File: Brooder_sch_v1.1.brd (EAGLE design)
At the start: 90 x 75 mm, 31 parts, among them J1 DCJ0202, J2 1X2-3.5MM, J3 DCJ0202, J4 1X2-3.5MM, U1 328P

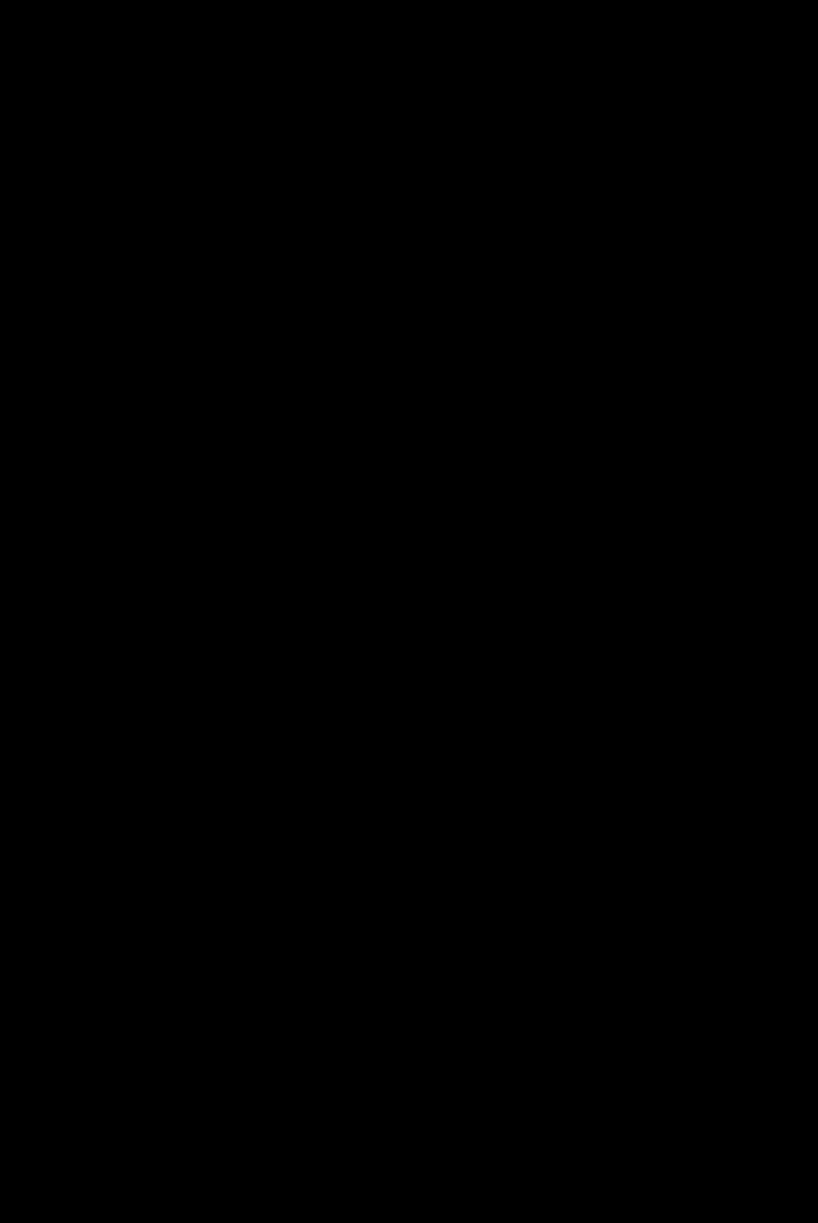
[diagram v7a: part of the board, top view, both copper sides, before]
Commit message: Adds extractor fan relay to schematic
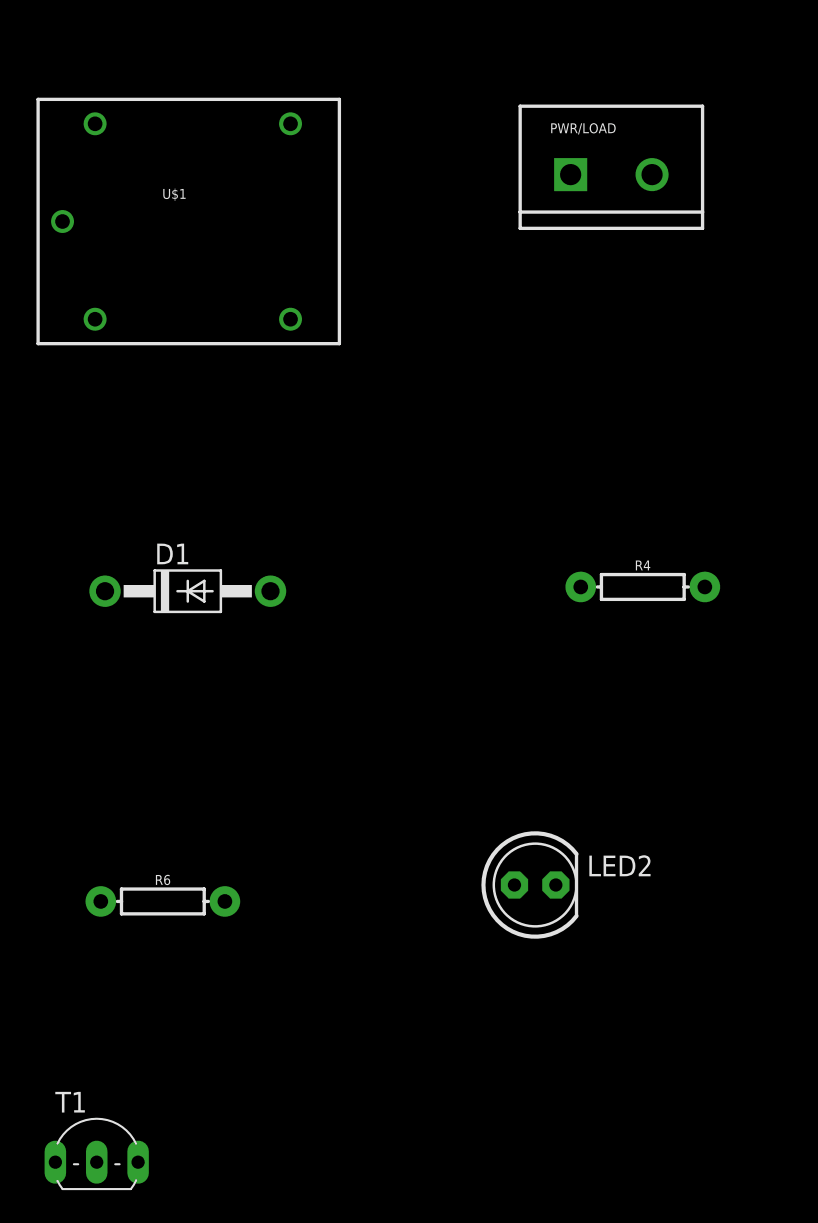
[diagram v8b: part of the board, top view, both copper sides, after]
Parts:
- added D1: 1N4007, adafruit:DO41-10
- added LED2: (no value), adafruit:LED5MM
- added PWR/LOAD: (no value), SparkFun-Connectors:SCREWTERMINAL-5MM-2
- added R4: 220, SparkFun-Resistors:AXIAL-0.3
- added R6: 1k, SparkFun-Resistors:AXIAL-0.3
- added T1: 2N2222, adafruit:TO92-EBC-OVAL
- added U$1: RELAYPTH, SRD-05VDC-SL-C:SRD-05VDC-SL-C
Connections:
- new net N$10: R6.P$1, T1.B
- new net N$13: PWR/LOAD.1, U$1.SWCLOSED
- new net N$14: PWR/LOAD.2, U$1.SWCOMMON
- new net N$6: D1.A, LED2.K, T1.C, U$1.COIL0
- new net N$7: LED2.A, R4.P$1
- net 5V: now also D1.C, R4.P$2, U$1.COIL1
- net GND: now also T1.E
- net PC1: now also R6.P$2
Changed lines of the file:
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@@
 <element name="R1" library="pot" library_urn="urn:adsk.eagle:library:331" package="CT6" package3d_urn="urn:adsk.eagle:package:22692/1" value="" x="14.57" y="58.36" rot="R270"/>
 <element name="JP1" library="pinhead" library_urn="urn:adsk.eagle:library:325" package="2X03" package3d_urn="urn:adsk.eagle:package:22462/2" value="" x="62.7" y="25.49" rot="R270"/>
+<element name="U$1" library="SRD-05VDC-SL-C" package="SRD-05VDC-SL-C" value="RELAYPTH" x="9.23" y="-24.48"/>
+<element name="D1" library="adafruit" package="DO41-10" value="1N4007" x="9.53" y="-47.3"/>
+<element name="T1" library="adafruit" package="TO92-EBC-OVAL" value="2N2222" x="3.94" y="-81.09"/>
+<element name="PWR/LOAD" library="SparkFun-Connectors" package="SCREWTERMINAL-5MM-2" value="" x="33.04" y="-21.72">
+<attribute name="SF_SKU" value="PRT-08432" x="4.96" y="-80.33" size="1.778" layer="27" display="off"/>
+</element>
+<element name="R4" library="SparkFun-Resistors" package="AXIAL-0.3" value="220" x="37.47" y="-47.04">
+<attribute name="PROD_ID" value="RES-09327" x="8" y="-99.89" size="1.778" layer="27" display="off"/>
+</element>
+<element name="R6" library="SparkFun-Resistors" package="AXIAL-0.3" value="1k" x="8" y="-66.35">
+<attribute name="PROD_ID" value="RES-09327" x="8" y="-118.69" size="1.778" layer="27" display="off"/>
+</element>
+<element name="LED2" library="adafruit" package="LED5MM" value="" x="30.86" y="-65.34"/>
 </elements>
 <signals>
@@
 <wire x1="72.1" y1="12.57" x2="70.81" y2="13.86" width="1.27" layer="16"/>
 <wire x1="70.81" y1="13.86" x2="67.58068125" y2="13.86" width="1.27" layer="16"/>
+<contactref element="T1" pad="E"/>
 <wire x1="15.02" y1="66.32" x2="34.4888" y2="66.7906" width="0" layer="19" extent="1-1"/>
 <wire x1="5" y1="7" x2="4.19" y2="14.85" width="0" layer="19" extent="16-16"/>
 <wire x1="20.24" y1="41.49" x2="13.87" y2="52.87" width="0" layer="19" extent="1-16"/>
 <wire x1="19.71" y1="34.8" x2="19.72" y2="39.62" width="0" layer="19" extent="1-1"/>
+<wire x1="1.4" y1="-82.36" x2="13" y2="2" width="0" layer="19" extent="16-16"/>
 </signal>
 <signal name="12V">
@@
 <wire x1="67.35" y1="62.01" x2="78.99" y2="62.01" width="1.27" layer="1"/>
 <wire x1="78.99" y1="62.01" x2="82.46" y2="58.54" width="1.27" layer="1"/>
+<contactref element="U$1" pad="COIL1"/>
+<contactref element="D1" pad="C"/>
+<contactref element="R4" pad="P$2"/>
+<wire x1="3.84" y1="-18.6" x2="4.45" y2="-47.3" width="0" layer="19" extent="1-1"/>
+<wire x1="41.28" y1="-47.04" x2="4.45" y2="-47.3" width="0" layer="19" extent="1-1"/>
+<wire x1="4.19" y1="19.93" x2="3.84" y2="-18.6" width="0" layer="19" extent="1-1"/>
 </signal>
 <signal name="N$5">
@@
 <wire x1="41.94" y1="46.37" x2="42.38" y2="46.81" width="1.27" layer="16"/>
 <wire x1="42.38" y1="46.81" x2="45" y2="46.81" width="1.27" layer="16"/>
+<contactref element="R6" pad="P$2"/>
+<wire x1="11.81" y1="-66.35" x2="41.94" y2="46.37" width="0" layer="19" extent="1-1"/>
 </signal>
 <signal name="PC4">
@@
 <wire x1="48.05" y1="26.05" x2="50.06" y2="24.04" width="1.27" layer="16"/>
 </signal>
+<signal name="N$6">
+<contactref element="D1" pad="A"/>
+<contactref element="U$1" pad="COIL0"/>
+<contactref element="LED2" pad="K"/>
+<contactref element="T1" pad="C"/>
+<wire x1="32.13" y1="-65.34" x2="6.48" y2="-82.36" width="0" layer="19" extent="1-1"/>
+<wire x1="14.61" y1="-47.3" x2="32.13" y2="-65.34" width="0" layer="19" extent="1-1"/>
+<wire x1="3.84" y1="-30.6" x2="14.61" y2="-47.3" width="0" layer="19" extent="1-1"/>
+</signal>
+<signal name="N$7">
+<contactref element="R4" pad="P$1"/>
+<contactref element="LED2" pad="A"/>
+<wire x1="33.66" y1="-47.04" x2="29.59" y2="-65.34" width="0" layer="19" extent="1-1"/>
+</signal>
+<signal name="N$10">
+<contactref element="R6" pad="P$1"/>
+<contactref element="T1" pad="B"/>
+<wire x1="4.19" y1="-66.35" x2="3.94" y2="-82.36" width="0" layer="19" extent="1-1"/>
+</signal>
+<signal name="N$13">
+<contactref element="PWR/LOAD" pad="1"/>
+<contactref element="U$1" pad="SWCLOSED"/>
+<wire x1="33.04" y1="-21.72" x2="15.84" y2="-30.6" width="0" layer="19" extent="1-1"/>
+</signal>
+<signal name="N$14">
+<contactref element="U$1" pad="SWCOMMON"/>
+<contactref element="PWR/LOAD" pad="2"/>
+<wire x1="38.04" y1="-21.72" x2="1.84" y2="-24.6" width="0" layer="19" extent="1-1"/>
+</signal>
 </signals>
